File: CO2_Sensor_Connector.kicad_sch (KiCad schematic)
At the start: 6 parts, among them J3 Conn_01x05, Q1 AO3400A, Q2 AO3401A

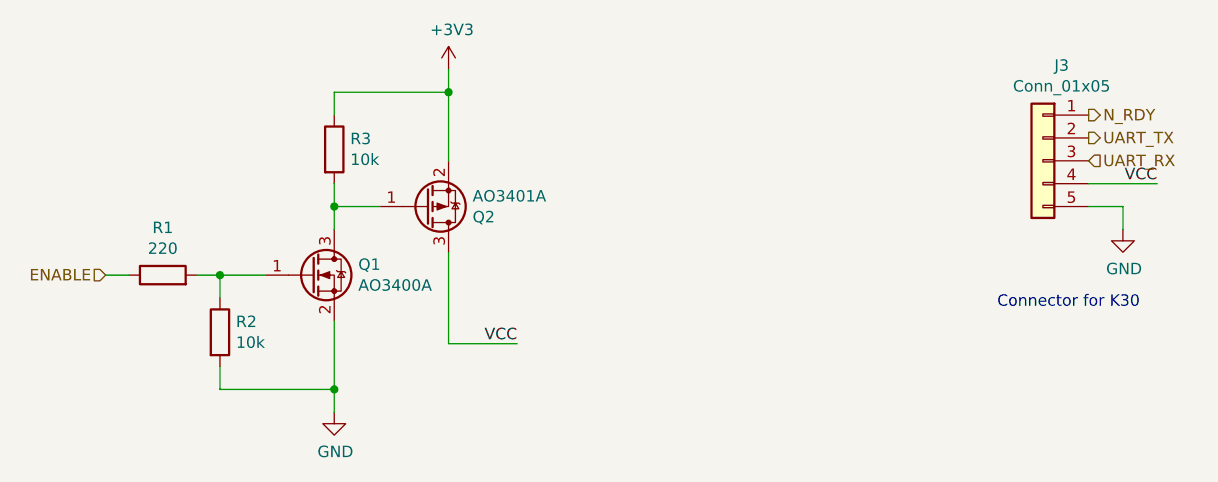
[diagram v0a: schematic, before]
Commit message: Move to KiCad v6, redesign circuit for chamber
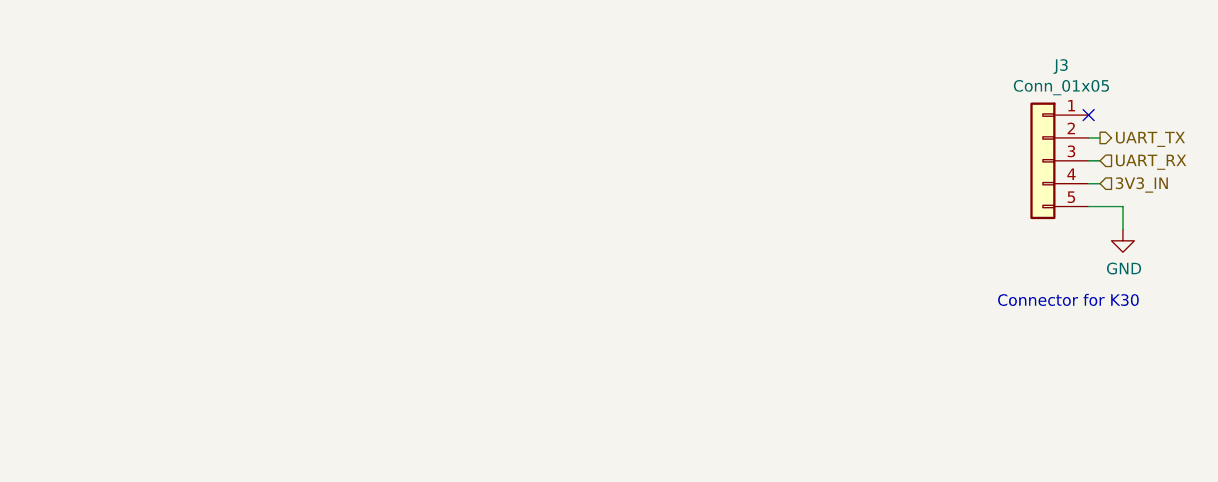
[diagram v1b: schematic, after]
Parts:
- removed Q1: AO3400A, Package_TO_SOT_SMD:SOT-23, symbol Transistor_FET:AO3400A
- removed Q2: AO3401A, Package_TO_SOT_SMD:SOT-23, symbol Transistor_FET:AO3401A
- removed R1: 220, Resistor_SMD:R_0603_1608Metric, symbol Device:R
- removed R2, R3: 10k, Resistor_SMD:R_0603_1608Metric, symbol Device:R
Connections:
- net N_RDY: no longer names the net of J3.1 (Pin_1)
- net VCC renamed 3V3_IN
- no-connect marks 0 -> 1
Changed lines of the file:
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@@
 (kicad_sch (version 20211123) (generator eeschema)
   (paper "A4")
-  (junction (at 109.22 119.38) (diameter 0) (color 0 0 0 0)
-  )
-  (junction (at 96.52 106.68) (diameter 0) (color 0 0 0 0)
-  )
-  (junction (at 109.22 99.06) (diameter 0) (color 0 0 0 0)
-  )
-  (junction (at 121.92 86.36) (diameter 0) (color 0 0 0 0)
-  )
-  (wire (pts (xy 109.22 86.36) (xy 121.92 86.36))
+  (no_connect (at 193.04 88.9))
+  (wire (pts (xy 194.31 96.52) (xy 193.04 96.52))
     (stroke (width 0) (type default) (color 0 0 0 0))
   )
-  (wire (pts (xy 109.22 111.76) (xy 109.22 119.38))
-    (stroke (width 0) (type default) (color 0 0 0 0))
-  )
-  (wire (pts (xy 96.52 119.38) (xy 109.22 119.38))
-    (stroke (width 0) (type default) (color 0 0 0 0))
-  )
-  (wire (pts (xy 86.36 106.68) (xy 83.82 106.68))
-    (stroke (width 0) (type default) (color 0 0 0 0))
-  )
-  (wire (pts (xy 121.92 86.36) (xy 121.92 93.98))
-    (stroke (width 0) (type default) (color 0 0 0 0))
-  )
-  (wire (pts (xy 121.92 86.36) (xy 121.92 83.82))
-    (stroke (width 0) (type default) (color 0 0 0 0))
-  )
-  (wire (pts (xy 93.98 106.68) (xy 96.52 106.68))
-    (stroke (width 0) (type default) (color 0 0 0 0))
-  )
-  (wire (pts (xy 96.52 109.22) (xy 96.52 106.68))
-    (stroke (width 0) (type default) (color 0 0 0 0))
-  )
-  (wire (pts (xy 109.22 88.9) (xy 109.22 86.36))
-    (stroke (width 0) (type default) (color 0 0 0 0))
-  )
-  (wire (pts (xy 96.52 119.38) (xy 96.52 116.84))
-    (stroke (width 0) (type default) (color 0 0 0 0))
-  )
-  (wire (pts (xy 121.92 114.3) (xy 129.54 114.3))
+  (wire (pts (xy 194.31 91.44) (xy 193.04 91.44))
     (stroke (width 0) (type default) (color 0 0 0 0))
   )
@@
     (stroke (width 0) (type default) (color 0 0 0 0))
   )
-  (wire (pts (xy 96.52 106.68) (xy 101.6 106.68))
-    (stroke (width 0) (type default) (color 0 0 0 0))
-  )
   (wire (pts (xy 196.85 101.6) (xy 196.85 99.06))
     (stroke (width 0) (type default) (color 0 0 0 0))
   )
-  (wire (pts (xy 109.22 119.38) (xy 109.22 121.92))
-    (stroke (width 0) (type default) (color 0 0 0 0))
-  )
-  (wire (pts (xy 109.22 99.06) (xy 114.3 99.06))
-    (stroke (width 0) (type default) (color 0 0 0 0))
-  )
-  (wire (pts (xy 109.22 99.06) (xy 109.22 101.6))
-    (stroke (width 0) (type default) (color 0 0 0 0))
-  )
-  (wire (pts (xy 193.04 96.52) (xy 200.66 96.52))
-    (stroke (width 0) (type default) (color 0 0 0 0))
-  )
-  (wire (pts (xy 109.22 96.52) (xy 109.22 99.06))
-    (stroke (width 0) (type default) (color 0 0 0 0))
-  )
-  (wire (pts (xy 121.92 104.14) (xy 121.92 114.3))
+  (wire (pts (xy 194.31 93.98) (xy 193.04 93.98))
     (stroke (width 0) (type default) (color 0 0 0 0))
   )
@@
     (effects (font (size 1.27 1.27)) (justify left bottom))
   )
-  (label "VCC" (at 200.66 96.52 180)
-    (effects (font (size 1.27 1.27)) (justify right bottom))
-  )
-  (label "VCC" (at 129.54 114.3 180)
-    (effects (font (size 1.27 1.27)) (justify right bottom))
-  )
-  (hierarchical_label "UART_RX" (shape input) (at 193.04 93.98 0)
+  (hierarchical_label "UART_RX" (shape input) (at 194.31 93.98 0)
     (effects (font (size 1.27 1.27)) (justify left))
   )
-  (hierarchical_label "N_RDY" (shape output) (at 193.04 88.9 0)
+  (hierarchical_label "3V3_IN" (shape input) (at 194.31 96.52 0)
     (effects (font (size 1.27 1.27)) (justify left))
   )
-  (hierarchical_label "UART_TX" (shape output) (at 193.04 91.44 0)
+  (hierarchical_label "UART_TX" (shape output) (at 194.31 91.44 0)
     (effects (font (size 1.27 1.27)) (justify left))
-  )
-  (hierarchical_label "ENABLE" (shape input) (at 83.82 106.68 180)
-    (effects (font (size 1.27 1.27)) (justify right))
-  )
-  (symbol (lib_id "Transistor_FET:AO3401A") (at 119.38 99.06 0) (mirror x) (unit 1)
-    (in_bom yes) (on_board yes)
-    (property "Reference" "Q2" (id 0) (at 124.587 100.2284 0)
-      (effects (font (size 1.27 1.27)) (justify left))
-    )
-    (property "Value" "AO3401A" (id 1) (at 124.587 97.917 0)
-      (effects (font (size 1.27 1.27)) (justify left))
-    )
-    (property "Footprint" "Package_TO_SOT_SMD:SOT-23" (id 2) (at 124.46 97.155 0)
-      (effects (font (size 1.27 1.27) italic) (justify left) hide)
-    )
-    (property "Datasheet" "http://www.aosmd.com/pdfs/datasheet/AO3401A.pdf" (id 3) (at 119.38 99.06 0)
-      (effects (font (size 1.27 1.27)) (justify left) hide)
-    )
-    (property "LCSC" "C15127" (id 4) (at 119.38 99.06 0)
-      (effects (font (size 1.27 1.27)) hide)
-    )
-    (pin "1")
-    (pin "2")
-    (pin "3")
-  )
-  (symbol (lib_id "Device:R") (at 90.17 106.68 90) (unit 1)
-    (in_bom yes) (on_board yes)
-    (property "Reference" "R1" (id 0) (at 90.17 101.4222 90))
-    (property "Value" "220" (id 1) (at 90.17 103.7336 90))
-    (property "Footprint" "Resistor_SMD:R_0603_1608Metric" (id 2) (at 90.17 108.458 90)
-      (effects (font (size 1.27 1.27)) hide)
-    )
-    (property "Datasheet" "~" (id 3) (at 90.17 106.68 0)
-      (effects (font (size 1.27 1.27)) hide)
-    )
-    (property "LCSC" "C22962" (id 4) (at 90.17 106.68 0)
-      (effects (font (size 1.27 1.27)) hide)
-    )
-    (pin "1")
-    (pin "2")
-  )
-  (symbol (lib_id "Device:R") (at 109.22 92.71 0) (unit 1)
-    (in_bom yes) (on_board yes)
-    (property "Reference" "R3" (id 0) (at 110.998 91.5416 0)
-      (effects (font (size 1.27 1.27)) (justify left))
-    )
-    (property "Value" "10k" (id 1) (at 110.998 93.853 0)
-      (effects (font (size 1.27 1.27)) (justify left))
-    )
-    (property "Footprint" "Resistor_SMD:R_0603_1608Metric" (id 2) (at 107.442 92.71 90)
-      (effects (font (size 1.27 1.27)) hide)
-    )
-    (property "Datasheet" "~" (id 3) (at 109.22 92.71 0)
-      (effects (font (size 1.27 1.27)) hide)
-    )
-    (property "LCSC" "C25804" (id 4) (at 109.22 92.71 0)
-      (effects (font (size 1.27 1.27)) hide)
-    )
-    (pin "1")
-    (pin "2")
-  )
-  (symbol (lib_id "power:+3V3") (at 121.92 83.82 0) (unit 1)
-    (in_bom yes) (on_board yes)
-    (property "Reference" "#PWR02" (id 0) (at 121.92 87.63 0)
-      (effects (font (size 1.27 1.27)) hide)
-    )
-    (property "Value" "+3V3" (id 1) (at 122.301 79.4258 0))
-    (property "Footprint" "" (id 2) (at 121.92 83.82 0)
-      (effects (font (size 1.27 1.27)) hide)
-    )
-    (property "Datasheet" "" (id 3) (at 121.92 83.82 0)
-      (effects (font (size 1.27 1.27)) hide)
-    )
-    (pin "1")
-  )
-  (symbol (lib_id "power:GND") (at 109.22 121.92 0) (unit 1)
-    (in_bom yes) (on_board yes)
-    (property "Reference" "#PWR01" (id 0) (at 109.22 128.27 0)
-      (effects (font (size 1.27 1.27)) hide)
-    )
-    (property "Value" "GND" (id 1) (at 109.347 126.3142 0))
-    (property "Footprint" "" (id 2) (at 109.22 121.92 0)
-      (effects (font (size 1.27 1.27)) hide)
-    )
-    (property "Datasheet" "" (id 3) (at 109.22 121.92 0)
-      (effects (font (size 1.27 1.27)) hide)
-    )
-    (pin "1")
-  )
-  (symbol (lib_id "Device:R") (at 96.52 113.03 0) (unit 1)
-    (in_bom yes) (on_board yes)
-    (property "Reference" "R2" (id 0) (at 98.298 111.8616 0)
-      (effects (font (size 1.27 1.27)) (justify left))
-    )
-    (property "Value" "10k" (id 1) (at 98.298 114.173 0)
-      (effects (font (size 1.27 1.27)) (justify left))
-    )
-    (property "Footprint" "Resistor_SMD:R_0603_1608Metric" (id 2) (at 94.742 113.03 90)
-      (effects (font (size 1.27 1.27)) hide)
-    )
-    (property "Datasheet" "~" (id 3) (at 96.52 113.03 0)
-      (effects (font (size 1.27 1.27)) hide)
-    )
-    (property "LCSC" "C25804" (id 4) (at 96.52 113.03 0)
-      (effects (font (size 1.27 1.27)) hide)
-    )
-    (pin "1")
-    (pin "2")
   )
   (symbol (lib_id "power:GND") (at 196.85 101.6 0) (unit 1)
@@
     (pin "1")
   )
-  (symbol (lib_id "Transistor_FET:AO3400A") (at 106.68 106.68 0) (unit 1)
-    (in_bom yes) (on_board yes)
-    (property "Reference" "Q1" (id 0) (at 111.887 105.5116 0)
-      (effects (font (size 1.27 1.27)) (justify left))
-    )
-    (property "Value" "AO3400A" (id 1) (at 111.887 107.823 0)
-      (effects (font (size 1.27 1.27)) (justify left))
-    )
-    (property "Footprint" "Package_TO_SOT_SMD:SOT-23" (id 2) (at 111.76 108.585 0)
-      (effects (font (size 1.27 1.27) italic) (justify left) hide)
-    )
-    (property "Datasheet" "http://www.aosmd.com/pdfs/datasheet/AO3400A.pdf" (id 3) (at 106.68 106.68 0)
-      (effects (font (size 1.27 1.27)) (justify left) hide)
-    )
-    (property "LCSC" "C20917" (id 4) (at 106.68 106.68 0)
-      (effects (font (size 1.27 1.27)) hide)
-    )
-    (pin "1")
-    (pin "2")
-    (pin "3")
-  )
   (symbol (lib_id "Connector_Generic:Conn_01x05") (at 187.96 93.98 0) (mirror y) (unit 1)

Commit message: Finalize schematic
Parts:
- renumbered J3 to J9
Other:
- note added: "Connector for SCD30"
- note removed: "Connector for K30"
- title: (none) -> CO2 Chamber - CO2 Sensor Connector
- moved on the sheet: J9
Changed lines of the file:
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@@
 (kicad_sch (version 20211123) (generator eeschema)
   (paper "A4")
-  (no_connect (at 193.04 88.9))
-  (wire (pts (xy 194.31 96.52) (xy 193.04 96.52))
+  (title_block
+    (title "CO2 Chamber - CO2 Sensor Connector")
+    (date "2022-05-20")
+    (rev "1")
+  )
+  (no_connect (at 153.67 90.17))
+  (wire (pts (xy 154.94 97.79) (xy 153.67 97.79))
     (stroke (width 0) (type default) (color 0 0 0 0))
   )
-  (wire (pts (xy 194.31 91.44) (xy 193.04 91.44))
+  (wire (pts (xy 154.94 92.71) (xy 153.67 92.71))
     (stroke (width 0) (type default) (color 0 0 0 0))
   )
-  (wire (pts (xy 193.04 99.06) (xy 196.85 99.06))
+  (wire (pts (xy 153.67 100.33) (xy 157.48 100.33))
     (stroke (width 0) (type default) (color 0 0 0 0))
   )
-  (wire (pts (xy 196.85 101.6) (xy 196.85 99.06))
+  (wire (pts (xy 157.48 102.87) (xy 157.48 100.33))
     (stroke (width 0) (type default) (color 0 0 0 0))
   )
-  (wire (pts (xy 194.31 93.98) (xy 193.04 93.98))
+  (wire (pts (xy 154.94 95.25) (xy 153.67 95.25))
     (stroke (width 0) (type default) (color 0 0 0 0))
   )
-  (text "Connector for K30" (at 182.88 110.49 0)
+  (text "Connector for SCD30\n" (at 143.51 111.76 0)
     (effects (font (size 1.27 1.27)) (justify left bottom))
   )
-  (hierarchical_label "UART_RX" (shape input) (at 194.31 93.98 0)
+  (hierarchical_label "UART_RX" (shape input) (at 154.94 95.25 0)
     (effects (font (size 1.27 1.27)) (justify left))
   )
-  (hierarchical_label "3V3_IN" (shape input) (at 194.31 96.52 0)
+  (hierarchical_label "3V3_IN" (shape input) (at 154.94 97.79 0)
     (effects (font (size 1.27 1.27)) (justify left))
   )
-  (hierarchical_label "UART_TX" (shape output) (at 194.31 91.44 0)
+  (hierarchical_label "UART_TX" (shape output) (at 154.94 92.71 0)
     (effects (font (size 1.27 1.27)) (justify left))
   )
-  (symbol (lib_id "power:GND") (at 196.85 101.6 0) (unit 1)
+  (symbol (lib_id "power:GND") (at 157.48 102.87 0) (unit 1)
     (in_bom yes) (on_board yes)
-    (property "Reference" "#PWR05" (id 0) (at 196.85 107.95 0)
+    (property "Reference" "#PWR027" (id 0) (at 157.48 109.22 0)
       (effects (font (size 1.27 1.27)) hide)
     )
-    (property "Value" "GND" (id 1) (at 196.977 105.9942 0))
-    (property "Footprint" "" (id 2) (at 196.85 101.6 0)
+    (property "Value" "GND" (id 1) (at 157.607 107.2642 0))
+    (property "Footprint" "" (id 2) (at 157.48 102.87 0)
       (effects (font (size 1.27 1.27)) hide)
     )
-    (property "Datasheet" "" (id 3) (at 196.85 101.6 0)
+    (property "Datasheet" "" (id 3) (at 157.48 102.87 0)
       (effects (font (size 1.27 1.27)) hide)
     )
     (pin "1")
   )
-  (symbol (lib_id "Connector_Generic:Conn_01x05") (at 187.96 93.98 0) (mirror y) (unit 1)
+  (symbol (lib_id "Connector_Generic:Conn_01x05") (at 148.59 95.25 0) (mirror y) (unit 1)
     (in_bom yes) (on_board yes)
-    (property "Reference" "J3" (id 0) (at 190.0428 83.3882 0))
-    (property "Value" "Conn_01x05" (id 1) (at 190.0428 85.6996 0))
-    (property "Footprint" "Connector_JST:JST_XH_B5B-XH-AM_1x05_P2.50mm_Vertical" (id 2) (at 187.96 93.98 0)
+    (property "Reference" "J9" (id 0) (at 150.6728 84.6582 0))
+    (property "Value" "Conn_01x05" (id 1) (at 150.6728 86.9696 0))
+    (property "Footprint" "Connector_JST:JST_XH_B5B-XH-AM_1x05_P2.50mm_Vertical" (id 2) (at 148.59 95.25 0)
       (effects (font (size 1.27 1.27)) hide)
     )
-    (property "Datasheet" "~" (id 3) (at 187.96 93.98 0)
+    (property "Datasheet" "~" (id 3) (at 148.59 95.25 0)
       (effects (font (size 1.27 1.27)) hide)
     )

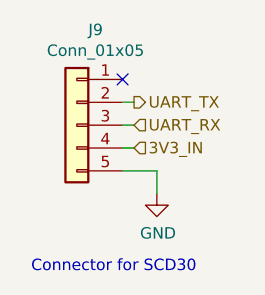
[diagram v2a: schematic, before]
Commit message: Finish PCB layout
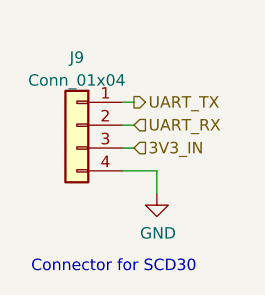
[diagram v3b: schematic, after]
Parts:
- removed J9: Conn_01x05, Connector_JST:JST_XH_B5B-XH-AM_1x05_P2.50mm_Vertical, symbol Connector_Generic:Conn_01x05
- added J9: Conn_01x04, Connector_JST:JST_XH_B4B-XH-A_1x04_P2.50mm_Vertical, symbol Connector_Generic:Conn_01x04
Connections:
- net 3V3_IN: now also J9.3 (Pin_3)
- net GND: now also J9.4 (Pin_4)
- net UART_RX: now also J9.2 (Pin_2)
- net UART_TX: now also J9.1 (Pin_1)
- no-connect marks 1 -> 0
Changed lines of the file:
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@@
     (rev "1")
   )
-  (no_connect (at 153.67 90.17))
   (wire (pts (xy 154.94 97.79) (xy 153.67 97.79))
     (stroke (width 0) (type default) (color 0 0 0 0))
@@
     (pin "1")
   )
-  (symbol (lib_id "Connector_Generic:Conn_01x05") (at 148.59 95.25 0) (mirror y) (unit 1)
-    (in_bom yes) (on_board yes)
-    (property "Reference" "J9" (id 0) (at 150.6728 84.6582 0))
-    (property "Value" "Conn_01x05" (id 1) (at 150.6728 86.9696 0))
-    (property "Footprint" "Connector_JST:JST_XH_B5B-XH-AM_1x05_P2.50mm_Vertical" (id 2) (at 148.59 95.25 0)
+  (symbol (lib_id "Connector_Generic:Conn_01x04") (at 148.59 95.25 0) (mirror y) (unit 1)
+    (in_bom yes) (on_board yes) (fields_autoplaced)
+    (property "Reference" "J9" (id 0) (at 148.59 87.7402 0))
+    (property "Value" "Conn_01x04" (id 1) (at 148.59 90.2771 0))
+    (property "Footprint" "Connector_JST:JST_XH_B4B-XH-A_1x04_P2.50mm_Vertical" (id 2) (at 148.59 95.25 0)
       (effects (font (size 1.27 1.27)) hide)
     )
     (property "Datasheet" "~" (id 3) (at 148.59 95.25 0)
+      (effects (font (size 1.27 1.27)) hide)
+    )
+    (property "LCSC" "C37815" (id 4) (at 148.59 95.25 0)
       (effects (font (size 1.27 1.27)) hide)
     )
@@
     (pin "3")
     (pin "4")
-    (pin "5")
   )
 )

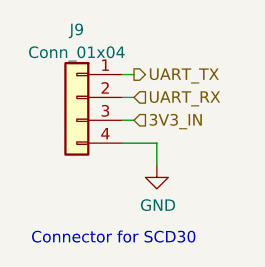
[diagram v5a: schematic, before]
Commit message: Add 5V boost converter and begin redesign of PCB
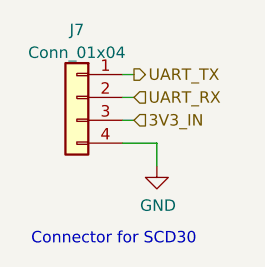
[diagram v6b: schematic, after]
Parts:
- renumbered J9 to J7
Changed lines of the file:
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@@
   (symbol (lib_id "power:GND") (at 157.48 102.87 0) (unit 1)
     (in_bom yes) (on_board yes)
-    (property "Reference" "#PWR033" (id 0) (at 157.48 109.22 0)
+    (property "Reference" "#PWR045" (id 0) (at 157.48 109.22 0)
       (effects (font (size 1.27 1.27)) hide)
     )
@@
   (symbol (lib_id "Connector_Generic:Conn_01x04") (at 148.59 95.25 0) (mirror y) (unit 1)
     (in_bom yes) (on_board yes) (fields_autoplaced)
-    (property "Reference" "J9" (id 0) (at 148.59 87.7402 0))
+    (property "Reference" "J7" (id 0) (at 148.59 87.7402 0))
     (property "Value" "Conn_01x04" (id 1) (at 148.59 90.2771 0))
     (property "Footprint" "Connector_JST:JST_XH_B4B-XH-A_1x04_P2.50mm_Vertical" (id 2) (at 148.59 95.25 0)

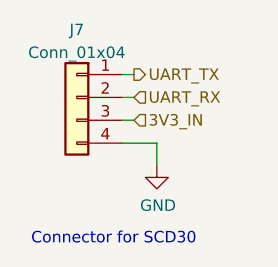
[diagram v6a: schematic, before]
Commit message: Finish component placement
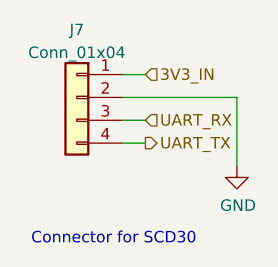
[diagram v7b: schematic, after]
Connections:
- net 3V3_IN: now also J7.1 (Pin_1); no longer J7.3 (Pin_3)
- net GND: now also J7.2 (Pin_2); no longer J7.4 (Pin_4)
- net UART_RX: now also J7.3 (Pin_3); no longer J7.2 (Pin_2)
- net UART_TX: now also J7.4 (Pin_4); no longer J7.1 (Pin_1)
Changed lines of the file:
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@@
     (rev "2")
   )
-  (wire (pts (xy 154.94 97.79) (xy 153.67 97.79))
+  (wire (pts (xy 153.67 92.71) (xy 156.21 92.71))
     (stroke (width 0) (type default) (color 0 0 0 0))
   )
-  (wire (pts (xy 154.94 92.71) (xy 153.67 92.71))
+  (wire (pts (xy 153.67 100.33) (xy 156.21 100.33))
     (stroke (width 0) (type default) (color 0 0 0 0))
   )
-  (wire (pts (xy 153.67 100.33) (xy 157.48 100.33))
+  (wire (pts (xy 166.37 95.25) (xy 153.67 95.25))
     (stroke (width 0) (type default) (color 0 0 0 0))
   )
-  (wire (pts (xy 157.48 102.87) (xy 157.48 100.33))
+  (wire (pts (xy 153.67 97.79) (xy 156.21 97.79))
     (stroke (width 0) (type default) (color 0 0 0 0))
   )
-  (wire (pts (xy 154.94 95.25) (xy 153.67 95.25))
+  (wire (pts (xy 166.37 95.25) (xy 166.37 102.87))
     (stroke (width 0) (type default) (color 0 0 0 0))
   )
@@
     (effects (font (size 1.27 1.27)) (justify left bottom))
   )
-  (hierarchical_label "UART_RX" (shape input) (at 154.94 95.25 0)
+  (hierarchical_label "UART_RX" (shape input) (at 156.21 97.79 0)
     (effects (font (size 1.27 1.27)) (justify left))
   )
-  (hierarchical_label "3V3_IN" (shape input) (at 154.94 97.79 0)
+  (hierarchical_label "3V3_IN" (shape input) (at 156.21 92.71 0)
     (effects (font (size 1.27 1.27)) (justify left))
   )
-  (hierarchical_label "UART_TX" (shape output) (at 154.94 92.71 0)
+  (hierarchical_label "UART_TX" (shape output) (at 156.21 100.33 0)
     (effects (font (size 1.27 1.27)) (justify left))
   )
-  (symbol (lib_id "power:GND") (at 157.48 102.87 0) (unit 1)
+  (symbol (lib_id "power:GND") (at 166.37 102.87 0) (unit 1)
     (in_bom yes) (on_board yes)
-    (property "Reference" "#PWR045" (id 0) (at 157.48 109.22 0)
+    (property "Reference" "#PWR045" (id 0) (at 166.37 109.22 0)
       (effects (font (size 1.27 1.27)) hide)
     )
-    (property "Value" "GND" (id 1) (at 157.607 107.2642 0))
-    (property "Footprint" "" (id 2) (at 157.48 102.87 0)
+    (property "Value" "GND" (id 1) (at 166.497 107.2642 0))
+    (property "Footprint" "" (id 2) (at 166.37 102.87 0)
       (effects (font (size 1.27 1.27)) hide)
     )
-    (property "Datasheet" "" (id 3) (at 157.48 102.87 0)
+    (property "Datasheet" "" (id 3) (at 166.37 102.87 0)
       (effects (font (size 1.27 1.27)) hide)
     )
